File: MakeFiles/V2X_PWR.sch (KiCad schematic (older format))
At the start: 65 parts, among them P10 Board Mount 2, P11 Ficudial2, P12 Board Mount 3, P13 Ficudial3, P15 Board Mount 4, P16 Ficudial4, P17 CUR_SEN, P18 CONN_02X10, P19 CUR_SEN, P25 Ficudial1, P27 Ficudial2, P28 Ficudial3, P29 Ficudial4, P6 Board Mount 1, P7 Ficudial1, P8 USB_A, P9 USB_u, Q11 IRF9335, Q13 BSS84, Q14 IRF9335, Q15 2N7000, SW2 SW_PUSH, U11 XRP6124, U12 SLG59M, U15 SLG59M, U16 SLG59M, U17 XRP6124, U18 SLG59M

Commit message: 53851 Import of V2X R2.0
capture from legacy repo
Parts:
- removed C50: 4U7, Custom Parts:C_0805_SM, symbol C
- removed C51: 560P, Custom Parts:C_0603_SM, symbol C
- removed C52: 10U, Custom Parts:C_1206_SM, symbol C
- removed D14: SBR3U30P1-7, Diodes_SMD:SOD-123, symbol D_Schottky_Small
- removed D15: MMSZ4678T1G, Diodes_SMD:SOD-123, symbol ZENER
- removed L5: 10U, Custom Parts:4.5x4.5mm_Ind, symbol INDUCTOR_SMALL
- removed P17, P19: CUR_SEN, Connect:PINHEAD1-2, symbol CONN_01X02
- removed P18: CONN_02X10, Pin_Headers:Pin_Header_Straight_2x10, symbol CONN_02X10
- removed P9: USB_u, Custom Parts:USB_Micro-B-DX4R005JJ2R1800, symbol USB_OTG
- removed Q13: BSS84, Custom Parts:SOT-23-123, symbol Q_PMOS_GSD
- removed Q14: IRF9335, Custom Parts:SOIC-8_MOS, symbol Q_PMOS_GSD
- removed Q15: 2N7000, Custom Parts:SOT-23-123, symbol Q_NMOS_SGD
- removed R10: DNS, Custom Parts:R_0603_sm, symbol R
- removed R11, R59, R67, R68, R76: 0, Custom Parts:R_0603_sm, symbol R
- removed R65, R75: 2K0, Custom Parts:R_0603_sm, symbol R
- removed R72: 6K2, Custom Parts:R_0603_sm, symbol R
- removed U12, U15, U16, U18: SLG59M, Custom Parts:STDFN-4, symbol SLG59M
- removed U17: XRP6124, Housings_SOT-23_SOT-143_TSOT-6:SOT-23-5, symbol XRP6124
- added C14, C21: 220U, Capacitors_SMD:c_elec_6.3x5.8, symbol CP
- added C16, C23, C27: 4U7, CustomParts:C_0805_SM, symbol C
- added C18, C25, C29, C32, C39, C40: 100N, CustomParts:C_0603_SM, symbol C
- added C22: 10N, CustomParts:C_0603_SM, symbol C
- added C26: 330P, CustomParts:C_0603_SM, symbol C
- added C28: 4U7, CustomParts:C_1206_SM, symbol C
- added C30, C31: 10U, CustomParts:C_1206_SM, symbol C
- added D10: SBR3U30P1-7, CustomParts:SOD-123, symbol D_Schottky_Small
- added D9: 4148, CustomParts:Diode_0805_12_SM, symbol D
- added FB2: 220, CustomParts:R_0603_sm, symbol FILTER
- added L2: 5U6, CustomParts:L_4.5x4.5, symbol INDUCTOR_SMALL
- added Q12: IRF9335, CustomParts:SOIC-8_MOS, symbol Q_PMOS_GSD
- added R45: 2K0, CustomParts:R_0603_sm, symbol R
- added R46: 10K, CustomParts:R_0603_sm, symbol R
- added R47: 8K2, CustomParts:R_0603_sm, symbol R
- added U10, U7: FDC6326L, TO_SOT_Packages_SMD:SOT-23-6, symbol Si1865DDL
- added U11, U12, U13: TLV70012DCK, TO_SOT_Packages_SMD:SOT-23-5, symbol TLV70012DCK
- added U9: XRP6124, TO_SOT_Packages_SMD:SOT-23-5, symbol XRP6124
- C13: renamed from C41; footprint Custom Parts:C_0603_SM -> CustomParts:C_0603_SM
- C15: renamed from C44; footprint Custom Parts:C_0603_SM -> CustomParts:C_0603_SM
- C17: renamed from C65; footprint Custom Parts:C_0603_SM -> CustomParts:C_0603_SM
- C19: renamed from C42; footprint Capacitors_Tantalum_SMD:TantalC_SizeD_EIA-7343_Reflow -> Capacitors_SMD:c_elec_6.3x5.8
- C20: renamed from C43; footprint Custom Parts:C_0805_SM -> CustomParts:C_1206_SM
- C24: renamed from C45; footprint Custom Parts:C_1206_SM -> CustomParts:C_1206_SM
- D8: renamed from D12; footprint Diodes_SMD:SOD-123 -> CustomParts:SOD-123
- L1: renamed from L3; footprint Custom Parts:4.5x4.5mm_Ind -> CustomParts:L_4.5x4.5
- P12: renamed from P25; footprint Fiducials:Fiducial_1mm_Dia_2.54mm_Outer_CopperTop -> Fiducials:Fiducial_1mm_Dia_2.54mm_Outer_CopperBottom
- P13: renamed from P27; footprint Fiducials:Fiducial_1mm_Dia_2.54mm_Outer_CopperTop -> Fiducials:Fiducial_1mm_Dia_2.54mm_Outer_CopperBottom
- P14: renamed from P28; footprint Fiducials:Fiducial_1mm_Dia_2.54mm_Outer_CopperTop -> Fiducials:Fiducial_1mm_Dia_2.54mm_Outer_CopperBottom
- P15: renamed from P29; footprint Fiducials:Fiducial_1mm_Dia_2.54mm_Outer_CopperTop -> Fiducials:Fiducial_1mm_Dia_2.54mm_Outer_CopperBottom
- P3: renamed from P8; footprint Connect:USB_A -> CustomParts:USB-A-SMT; Mouse PN 523-UE27AC5410H -> 806-KUSSMT2AS1NBTR
- Q11: footprint Custom Parts:SOIC-8_MOS -> CustomParts:SOIC-8_MOS
- R37: renamed from R69; value 2K0 -> 10K; footprint Custom Parts:R_0603_sm -> CustomParts:R_0603_sm; Mouse PN 71-CRCW0603-2.0k-E3 -> 71-CRCW0603-10K-E3
- R38: renamed from R73; value 10K -> 24K; footprint Custom Parts:R_0603_sm -> CustomParts:R_0603_sm; Mouse PN 71-CRCW0603-10k-E3 -> 71-CRCW0603-24k-E3
- R39: renamed from R61; footprint Custom Parts:R_0603_sm -> CustomParts:R_0603_sm
- R40: renamed from R62; footprint Custom Parts:R_0603_sm -> CustomParts:R_0603_sm
- R41: renamed from R71; value 2K0 -> 10K; footprint Custom Parts:R_0603_sm -> CustomParts:R_0603_sm; Mouse PN 71-CRCW0603-2.0k-E3 -> 71-CRCW0603-10K-E3
- R42: renamed from R66; footprint Custom Parts:R_0603_sm -> CustomParts:R_0603_sm
- R43: renamed from R74; footprint Custom Parts:R_0603_sm -> CustomParts:R_0603_sm
- R44: renamed from R70; value 10K -> 24K; footprint Custom Parts:R_0603_sm -> CustomParts:R_0603_sm; Mouse PN 71-CRCW0603-10k-E3 -> 71-CRCW0603-24k-E3
- R51: renamed from R88; footprint Custom Parts:R_0603_sm -> CustomParts:R_0603_sm
- R52: renamed from R89; footprint Custom Parts:R_0603_sm -> CustomParts:R_0603_sm
- SW2: footprint Custom Parts:PTS645VK58-2-LFS -> CustomParts:PTS645VK58-2-LFS; Mouse PN 506-FSMSM -> PTS645VK39-2-LFS
- U8: renamed from U11; footprint Housings_SOT-23_SOT-143_TSOT-6:SOT-23-5 -> TO_SOT_Packages_SMD:SOT-23-5
- renumbered D11 to D6, D10 to D7, P13 to P10, P16 to P11, P6 to P4, P10 to P5, P12 to P6, P15 to P7, P7 to P8, P11 to P9
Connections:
- net 12V0_B: now also R37.2, C28.1, C39.1, Q12.2 (S), U13.1 (IN), U7.4 (S2), U9.5 (VIN); no longer R37.1
- net 3V3_EN: now also U13.3 (EN)
- net 4V1_EN: now also D9.2 (A)
- net 5V0_A: now also C15.1, C24.1, L1.2, R40.2, R46.1, U10.4 (S2)
- net 5V0_B: now also U10.2 (D2), U10.3 (D2)
- net 5V0_B_EN: now also U10.5 (EN)
- net GND: now also C14.2, C16.2, C18.2, C21.2, C22.2, C23.2, C25.2, C27.2, C28.2, C29.2, C30.2, C31.2, C32.2, C39.2, C40.2, D10.2 (A), R45.1, U10.1 (R2), U11.2 (GND), U12.2 (GND), U13.2 (GND), U7.1 (R2), U9.2 (GND)
- net at R42.1, R44.2: now also D9.1 (K), U9.1 (EN)
- net at R38.2, R41.1, SW2.1: now also U7.5 (EN)
- net at R42.2: now also U7.2 (D2), U7.3 (D2)
- new net: R37.1, U7.6 (R1C1)
- new net: R46.2, U10.6 (R1C1)
- new net: C26.2, R45.2, R47.2, U9.3 (FB)
- new net: D10.1 (K), L2.1, Q12.3 (D)
- new net: Q12.1 (G), U9.4 (GATE)
- new net 3V3: C32.1, C40.1, U12.5 (OUT), U13.5 (OUT)
- new net 3V3F1: C27.1, U11.5 (OUT)
- new net 4V1: C14.1, C16.1, C18.1, C26.1, C29.1, C30.1, C31.1, FB2.2, L2.2, R47.1, U12.1 (IN), U12.3 (EN)
- new net 4V1F1: C21.1, C22.1, C23.1, C25.1, FB2.1, U11.1 (IN)
- new net GPS_EN: U11.3 (EN)
- no-connect marks 15 -> 14
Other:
- note added: "4.1V @ 1.5A DC-DC Power Supply"
- note added: "5V @ 1A DC-DC Power Supply"
- note added: "Button starts the 4V1 -> 3V3 supplies\nMust hold 4V1_EN high to stay on\nBUTTON is input signal once running"
- note removed: "3.3V @ 1A DC-DC Power Supply"
- note removed: "5V @ 1.25A DC-DC Power Supply"
- note removed: "Accelerometer 3V3 rail"
- note removed: "Button force starts the 3V3 to start SEQ\nSEQ must hold 3V3_EN high to stay on\nBUTTON is soft button signal once running\n3V3_EN pulled low kills supply regaurdless if button pressed"
- note removed: "CAN 3V3 rail"
- note removed: "GSM+GPS board header"
- note removed: "HUB & FTDI 3V3 rail"
- note removed: "HUB Data, HOST Power"
- note removed: "SEQ side"
- note removed: "SEQ will disable the 3V3 Supply\nand siphon power from 4V1 while \nin SMS standby recieve power state."
- note removed: "Slew Rate is\nControlable"
- moved on the sheet: C13, C15, C17, C19, C20, C24, D6, D7, D8, F1, F2, L1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

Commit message: Changes for documentation
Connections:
- net BUTTON: now also C17.1; no longer C17.2
- net GND: now also C17.2; no longer C17.1
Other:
- moved on the sheet: C13, C17, C19, C26, C28, C29, C30, C31, C32, C39, C40, D10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

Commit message: Updated Xtal footprint
16 & 24mhz crystal footprints were too small
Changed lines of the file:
@@
 LIBS:Zilog
 LIBS:CUSTOM_KICAD_PART
+LIBS:sim5320_KICAD_PART
 LIBS:V2X-cache
 EELAYER 25 0
@@
 Connection ~ 1800 1000
 Wire Wire Line
-	2400 1000 2500 1000
-Wire Wire Line
-	2500 1000 2600 1000
+	2400 1000 2600 1000
 Wire Wire Line
 	2500 1000 2500 1050
@@
 5V0_EN
 Wire Wire Line
-	2500 2300 2800 2300
-Wire Wire Line
-	2800 2300 3050 2300
+	2500 2300 3050 2300
 Wire Wire Line
 	3050 2300 3050 2150
@@
 	2800 2700 2800 2800
 Wire Wire Line
-	2700 2800 2800 2800
-Wire Wire Line
-	2800 2800 2900 2800
+	2700 2800 2900 2800
 Connection ~ 2800 2800
 $Comp
@@
 $EndComp
 Wire Wire Line
-	3400 2800 3500 2800
-Wire Wire Line
-	3500 2800 3700 2800
+	3400 2800 3700 2800
 Wire Wire Line
 	3700 2800 3700 2650
@@
 	3500 3050 3500 2800
 Wire Wire Line
-	1950 3050 2050 3050
-Wire Wire Line
-	2050 3050 3500 3050
+	1950 3050 3500 3050
 Connection ~ 3500 2800
 Wire Wire Line
@@
 	1650 3050 1600 3050
 Wire Wire Line
-	1600 3050 1600 2800
-Wire Wire Line
-	1500 2800 1550 2800
-Wire Wire Line
-	1550 2800 1600 2800
-Wire Wire Line
-	1600 2800 1650 2800
+	1600 2800 1600 3050
+Wire Wire Line
+	1500 2800 1650 2800
 Connection ~ 1600 2800
 Wire Wire Line
@@
 Connection ~ 5200 4000
 Wire Wire Line
-	2500 4300 2850 4300
-Wire Wire Line
-	2850 4300 3100 4300
-Wire Wire Line
-	3100 4300 3700 4300
+	2500 4300 3700 4300
 Text Notes 950  6150 0    69   ~ 0
 Button starts the 4V1 -> 3V3 supplies\nMust hold 4V1_EN high to stay on\nBUTTON is input signal once running
@@
 	5200 4000 5200 4050
 Wire Wire Line
-	4700 4000 4750 4000
-Wire Wire Line
-	4750 4000 4800 4000
+	4700 4000 4800 4000
 Wire Wire Line
 	4750 4000 4750 4150
@@
 $EndComp
 Wire Wire Line
-	5500 2450 5550 2450
-Wire Wire Line
-	5550 2450 5600 2450
+	5500 2450 5600 2450
 Wire Wire Line
 	5550 2450 5550 2600
@@
 Connection ~ 5550 2450
 Wire Wire Line
-	4200 2300 4200 2450
-Wire Wire Line
-	4200 2450 4200 2600
+	4200 2300 4200 2600
 Wire Wire Line
 	4200 2450 4500 2450
 Connection ~ 4200 2450
 Wire Wire Line
-	3400 4000 3700 4000
+	3200 4000 3700 4000
 $Comp
 L FILTER FB2
@@
 Connection ~ 3350 7000
 Wire Wire Line
-	2900 7000 3050 7000
-Wire Wire Line
-	3050 7000 3350 7000
-Wire Wire Line
-	3350 7000 3650 7000
-Wire Wire Line
-	3650 7000 4100 7000
-Wire Wire Line
-	4100 7000 4650 7000
+	2900 7000 4650 7000
 $Comp
 L GND #PWR054
@@
 	3650 7050 3650 7000
 Wire Wire Line
-	1500 6900 1500 7000
-Wire Wire Line
-	1500 7000 1500 7050
-Wire Wire Line
-	1500 7000 1800 7000
-Wire Wire Line
-	1800 7000 2100 7000
-Wire Wire Line
-	2100 7000 2200 7000
+	1500 6900 1500 7050
+Wire Wire Line
+	1500 7000 2200 7000
 Wire Wire Line
 	1800 7050 1800 7000
@@
 4V1
 Wire Wire Line
-	8150 4300 8450 4300
-Wire Wire Line
-	8450 4300 8700 4300
+	8150 4300 8700 4300
 Wire Wire Line
 	8700 4300 8700 4150
@@
 	8450 4700 8450 4800
 Wire Wire Line
-	8350 4800 8450 4800
-Wire Wire Line
-	8450 4800 8550 4800
+	8350 4800 8550 4800
 Connection ~ 8450 4800
 Wire Wire Line
-	9050 4800 9150 4800
-Wire Wire Line
-	9150 4800 9350 4800
-Wire Wire Line
-	9350 4800 9600 4800
+	9050 4800 9600 4800
 Wire Wire Line
 	9150 5050 9150 4800
 Wire Wire Line
-	7600 5050 7700 5050
-Wire Wire Line
-	7700 5050 9150 5050
+	7600 5050 9150 5050
 Connection ~ 9150 4800
 Wire Wire Line
@@
 	7300 5050 7250 5050
 Wire Wire Line
-	7250 5050 7250 4800
-Wire Wire Line
-	7150 4800 7200 4800
-Wire Wire Line
-	7200 4800 7250 4800
-Wire Wire Line
-	7250 4800 7300 4800
+	7250 4800 7250 5050
+Wire Wire Line
+	7150 4800 7300 4800
 Connection ~ 7250 4800
 Wire Wire Line
@@
 $EndComp
 Wire Wire Line
-	8600 5800 8600 5900
-Wire Wire Line
-	8600 5900 8600 6050
-Wire Wire Line
-	8600 6050 8600 6100
+	8600 5800 8600 6100
 Wire Wire Line
 	8600 6050 8700 6050
@@
 Connection ~ 8600 5900
 Wire Wire Line
-	9700 5800 9700 5900
-Wire Wire Line
-	9700 5900 9700 6100
+	9700 5800 9700 6100
 Wire Wire Line
 	9700 5900 9600 5900
@@
 $EndComp
 Wire Wire Line
-	5100 4000 5200 4000
-Wire Wire Line
-	5200 4000 5450 4000
-Wire Wire Line
-	5450 4000 5600 4000
+	5100 4000 5600 4000
 Wire Wire Line
 	5450 4000 5450 4300
@@
 $EndComp
 Wire Wire Line
-	4100 6900 4100 7000
-Wire Wire Line
-	4100 7000 4100 7050
+	4100 6900 4100 7050
 Text GLabel 4100 6900 1    60   Input ~ 0
 4V1F1
 Connection ~ 4100 7000
 Wire Wire Line
-	5650 6900 5650 7000
-Wire Wire Line
-	5650 7000 5650 7050
+	5650 6900 5650 7050
 Wire Wire Line
 	5650 7000 5550 7000
@@
 $EndComp
 Wire Wire Line
-	6650 5800 6650 5900
-Wire Wire Line
-	6650 5900 6650 6100
+	6650 5800 6650 6100
 Wire Wire Line
 	6650 5900 7100 5900
 Connection ~ 6650 5900
 Wire Wire Line
-	8100 5800 8100 5900
-Wire Wire Line
-	8100 5900 8100 6100
+	8100 5800 8100 6100
 Wire Wire Line
 	8100 5900 8000 5900
@@
 Connection ~ 3100 4300
 Wire Wire Line
-	3100 4800 3100 4900
-Wire Wire Line
-	3100 4900 3100 5000
+	3100 4800 3100 5000
 Wire Wire Line
 	3200 4900 3100 4900
@@
 Connection ~ 3400 4000
 Wire Wire Line
-	3200 4000 3400 4000
-Wire Wire Line
 	3400 4000 3400 4150

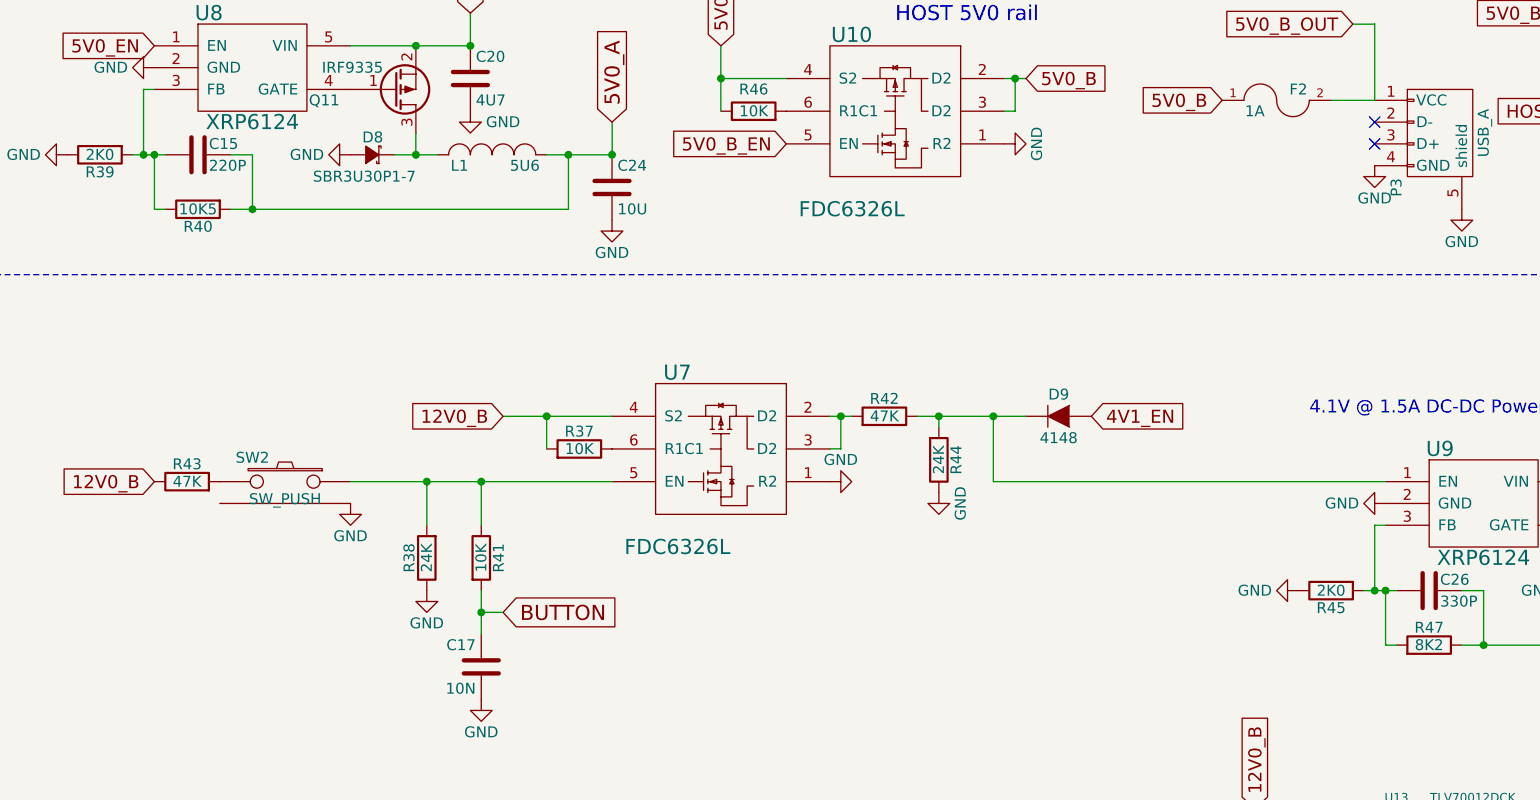
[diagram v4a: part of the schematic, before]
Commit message: Part numer updates
for error or out of stock
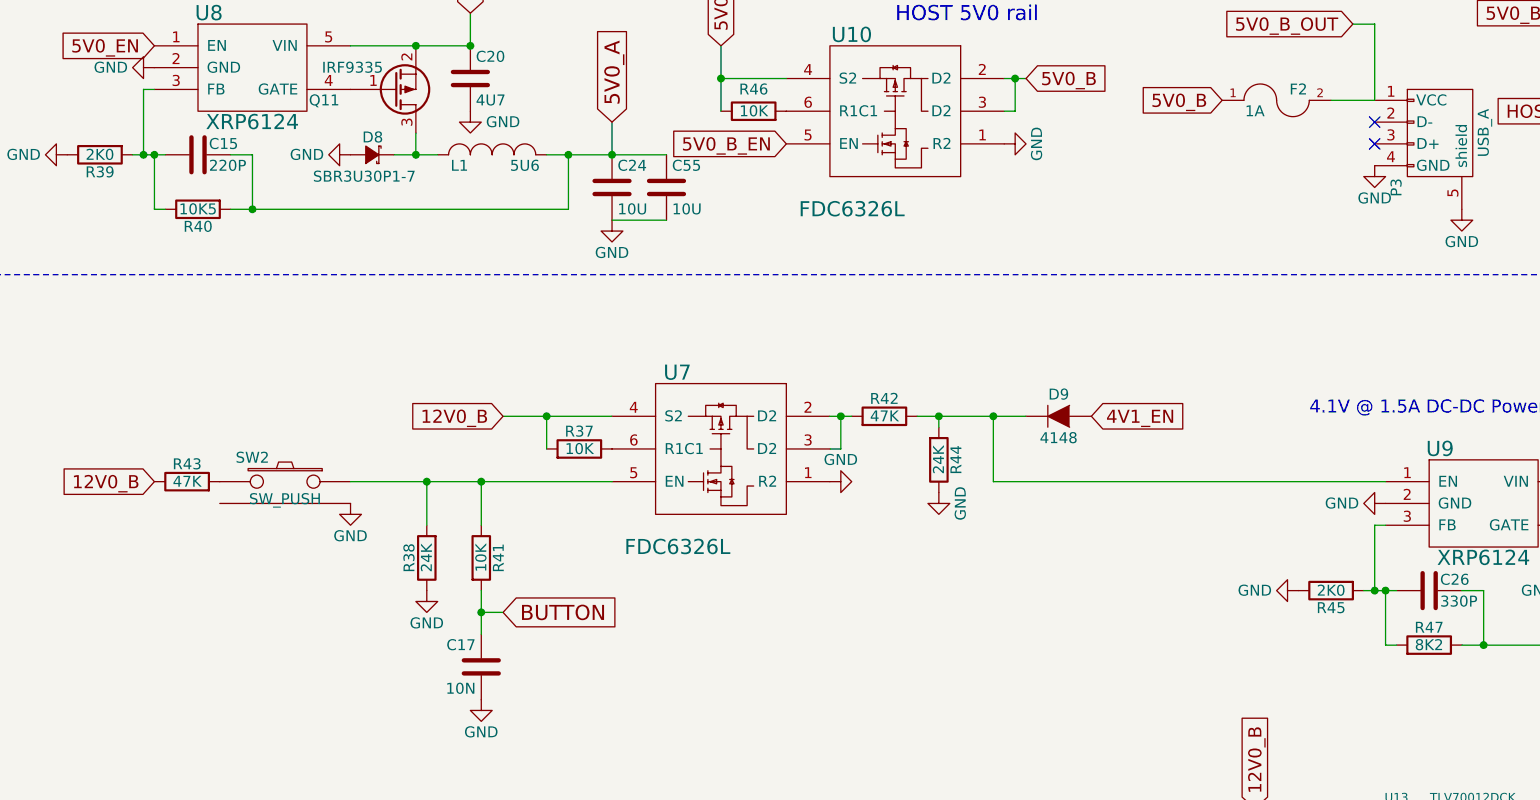
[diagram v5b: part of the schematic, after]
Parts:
- added C55: 10U, CustomParts:C_1206_SM, symbol C
- F1: Mouse PN 530-0ZCG0110AF2C -> 530-0ZCG0160BF2C
- F2: Mouse PN 530-0ZCC0125FF2C -> 530-0ZCG0200AF2B
- P3: Mouse PN 806-KUSSMT2AS1NBTR -> 806-KUSBEX-SMT2AS1N
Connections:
- net 5V0_A: now also C55.1
- net GND: now also C55.2

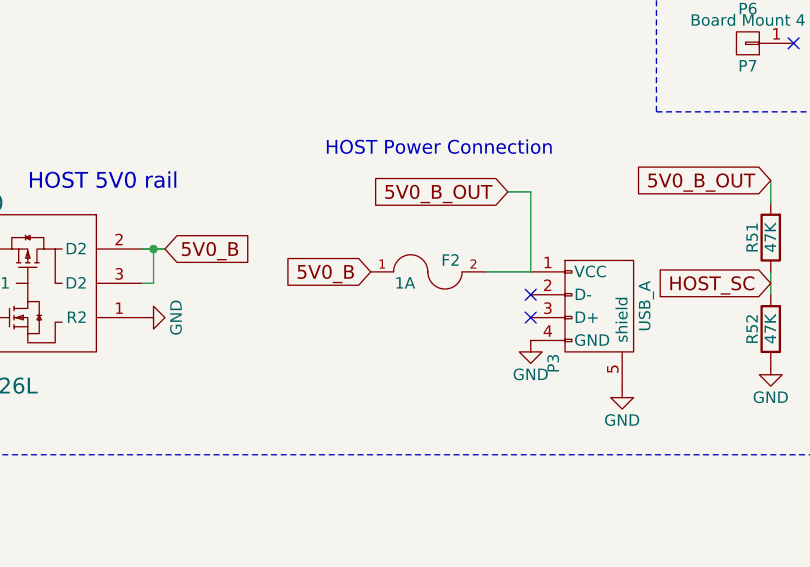
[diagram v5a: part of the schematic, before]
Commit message: Rev2.1 produced
Built R2.0, included findings, minor tweaks to placment and BOM.
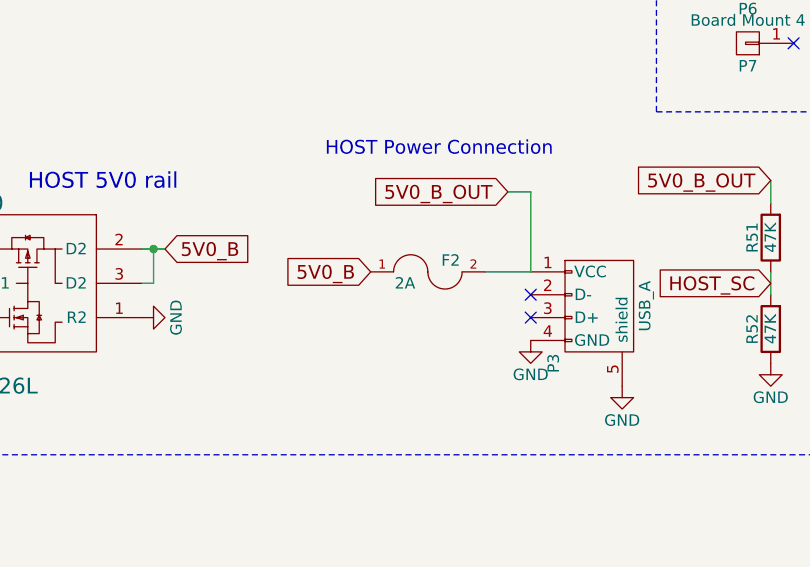
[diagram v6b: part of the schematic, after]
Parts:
- C14, C21: Mouse PN 710-875105244013 -> 667-10SVPE220M
- C16, C23, C27: Mouse PN 581-12063C475KAT2A -> 81-GRM21BR71A475KA3K
- F2: value 1A -> 2A
- U10, U7: Mouse PN (none) -> 512-FDC6326L
- U11, U12, U13: Mouse TLV70012DCK -> (none); Mouse PN (none) -> 511-LDK320M33R
